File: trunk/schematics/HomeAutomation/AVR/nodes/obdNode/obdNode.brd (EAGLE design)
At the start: 37.4 x 24 mm, 30 parts, among them IC1 MCP2515, IC2 TH8056KDC-AAA-008-RE, IC3 AMIS42665, IC4 ATMEGA64-TQFP32TQFP32, IC5 LM2674, X1 AVRISP6PINHEADER, X2 MICROMATCH-6

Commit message: Work on obdNode
git-svn-id: http://svn.arune.se/svn/hardware@888 bbe6898a-5d1e-0410-8d97-fea9c15d82f3
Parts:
- added C4: 100n, rcl:C0402
- R1, R4: value 10k -> (none)
- moved C12 2.24 mm to (26.0, 42.7)
- moved IC1 2.24 mm to (21.2, 39.9)
- moved R1 2.24 mm to (26.0, 41.6)
- moved IC5 0.71 mm to (32.1, 35.5)
- moved L1 0.41 mm to (38.5, 37.1)
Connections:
- net GND: now also C4.2
- net VBAT: now also C4.1
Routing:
- net GND: track 31.7 -> 36.2 mm, vias 36 -> 38
- net MISO: track 19.8 -> 17.6 mm
- net VBAT: track 26.4 -> 24.9 mm, vias 1 -> 0
- net CLK: track 5.63 -> 4.70 mm
- net CS: track 20.6 -> 19.6 mm
- net SCK: track 17.7 -> 16.7 mm
- net MOSI: track 25.6 -> 24.7 mm
- net INT: track 24.5 -> 23.5 mm
- net TXCAN2: track 12.1 -> 11.2 mm
- net VCC: track 74.6 -> 75.2 mm
- net RXCAN2: track 18.9 -> 18.4 mm

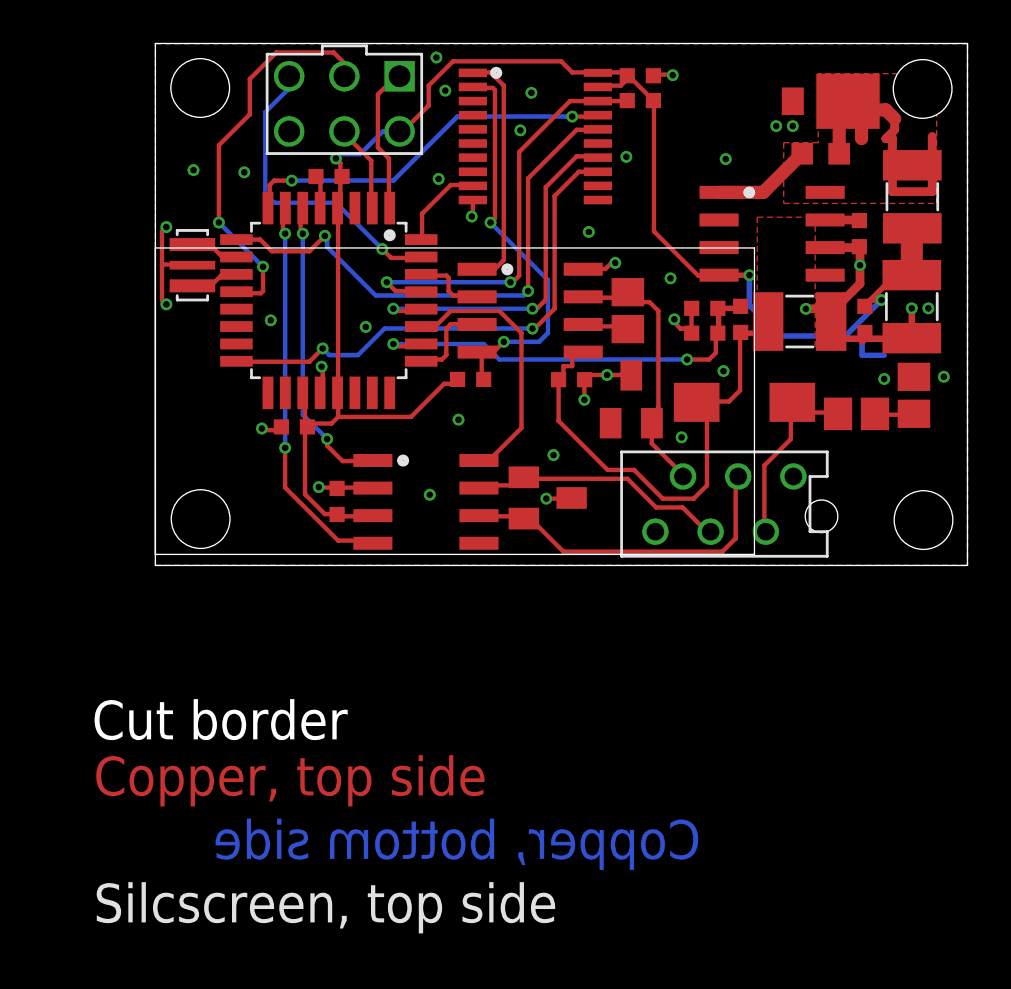
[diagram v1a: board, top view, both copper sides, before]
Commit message: Minor layout improvements
git-svn-id: http://svn.arune.se/svn/hardware@889 bbe6898a-5d1e-0410-8d97-fea9c15d82f3
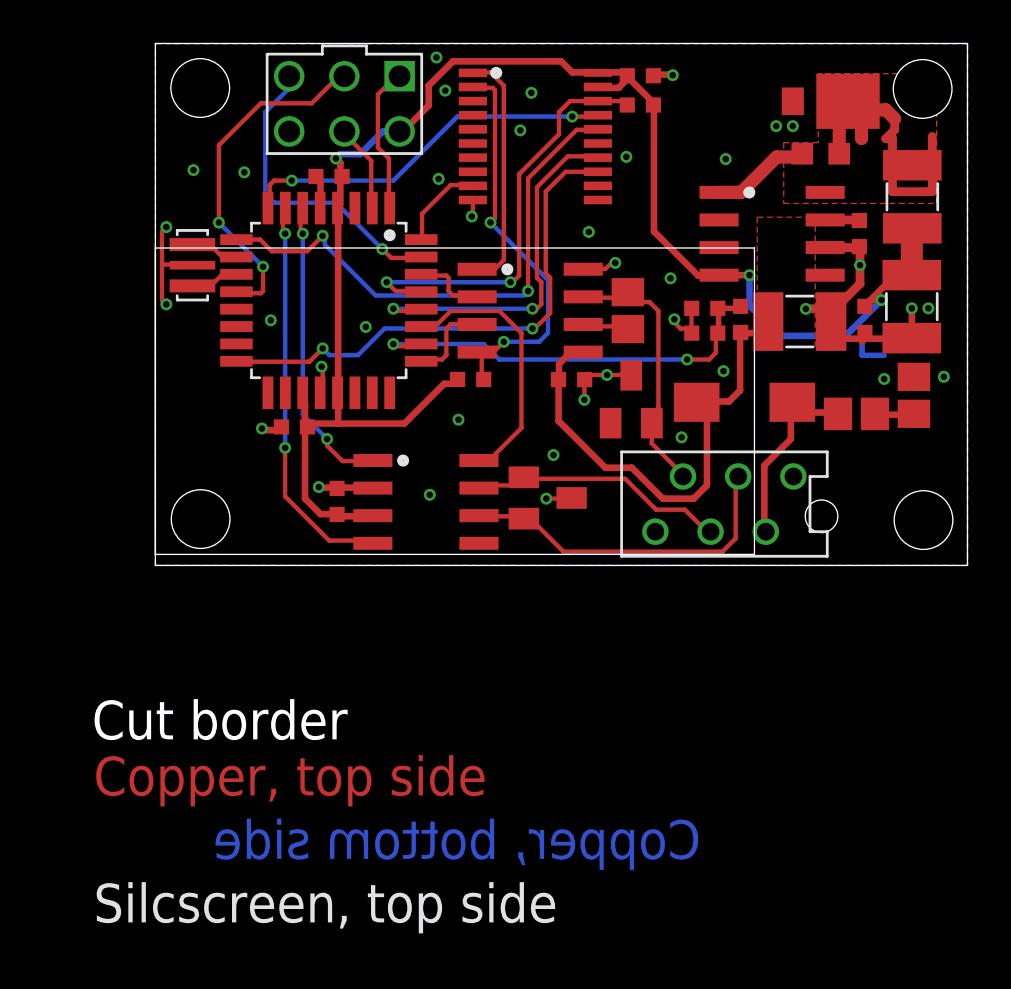
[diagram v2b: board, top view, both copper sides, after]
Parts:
- moved R1 0.20 mm to (26.0, 41.4)
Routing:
- net SCK_A: track 18.2 -> 16.0 mm
- net VCC: track 75.2 -> 75.9 mm
- net INT: track 23.5 -> 24.1 mm

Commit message: Updated version of core module with  - a cheaper PSU  - ISP-contacts as board-edge-connectors
git-svn-id: http://svn.arune.se/svn/hardware@891 bbe6898a-5d1e-0410-8d97-fea9c15d82f3
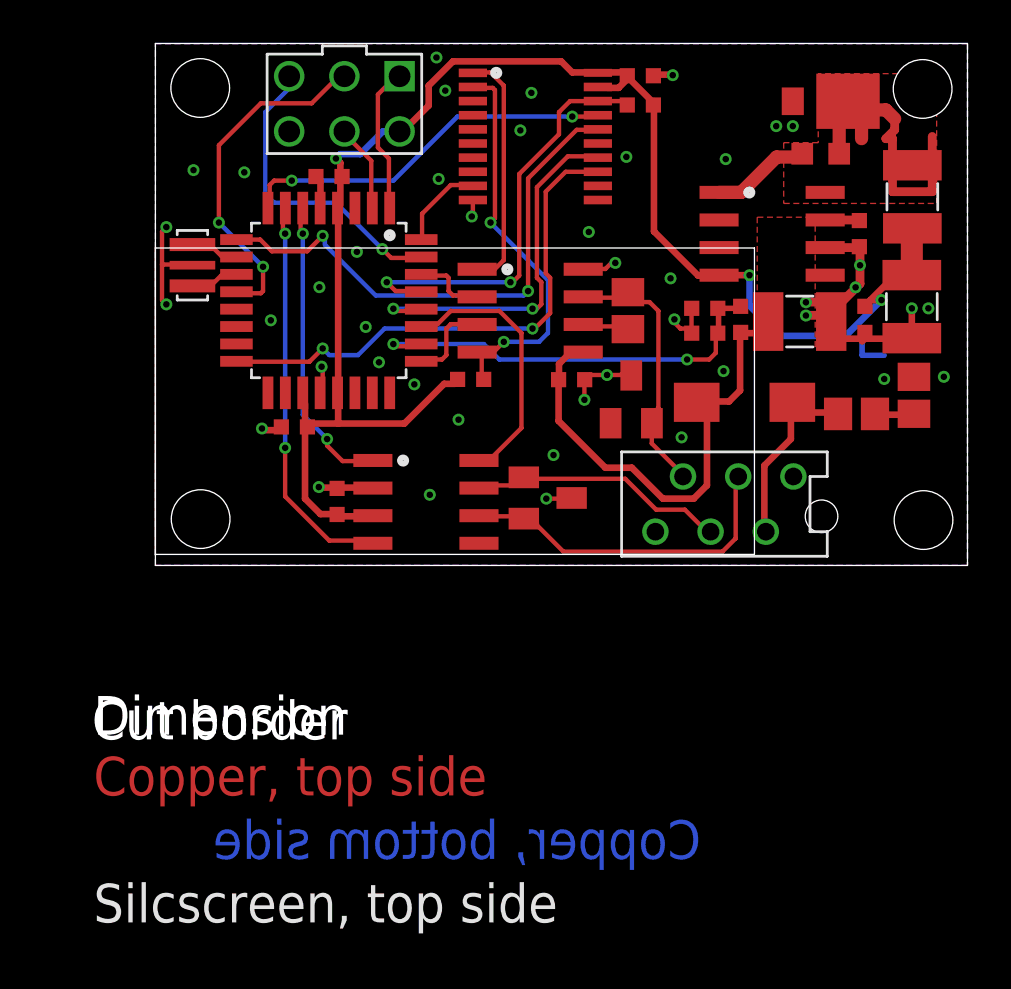
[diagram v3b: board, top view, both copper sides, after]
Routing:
- net GND: track 36.2 -> 37.3 mm, vias 38 -> 44
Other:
- board text added: "Dimension"
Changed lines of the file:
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@@
 <wire x1="36.431" y1="36.4744" x2="35.669" y2="36.4744" width="0.0762" layer="49"/>
 <wire x1="35.669" y1="36.4744" x2="35.669" y2="34.4424" width="0.0762" layer="49"/>
+<text x="0.8382" y="12.4079" size="1.778" layer="20" ratio="10">Dimension</text>
 </plain>
 <attributes>
@@
 <wire x1="36.195" y1="29.863" x2="36.195" y2="30.625" width="0.254" layer="16"/>
 <wire x1="36.195" y1="29.863" x2="37.211" y2="29.863" width="0.254" layer="16"/>
-<via x="33.609" y="31.995" extent="1-16" drill="0.3"/>
+<via x="33.609" y="32.2998" extent="1-16" drill="0.3"/>
 <via x="33.006" y="40.404" extent="1-16" drill="0.3"/>
 <via x="36.0982" y="34.0032" extent="1-16" drill="0.3"/>
@@
 <via x="27.4828" y="42.7482" extent="1-16" drill="0.3"/>
 <via x="16.7132" y="37.973" extent="1-16" drill="0.3"/>
-<polygon width="0.2032" layer="16" isolate="0.1524" rank="3">
+<polygon width="0.2032" layer="16" isolate="0.2032" rank="3">
 <vertex x="41.042" y="44.198"/>
 <vertex x="41.042" y="20.201"/>
@@
 <vertex x="3.683" y="44.198"/>
 </polygon>
-<polygon width="0.2032" layer="1" isolate="0.1524" rank="3">
+<polygon width="0.2032" layer="1" isolate="0.2032" rank="3">
 <vertex x="41.042" y="44.198"/>
 <vertex x="41.042" y="20.201"/>
@@
 <wire x1="36.0982" y1="34.8282" x2="36.0982" y2="33.1518" width="0.4064" layer="1"/>
 <wire x1="36.0982" y1="33.1518" x2="34.8488" y2="31.9024" width="0.4064" layer="1"/>
-<wire x1="33.6296" y1="32.004" x2="34.7472" y2="32.004" width="0.4064" layer="1"/>
+<wire x1="33.6296" y1="32.3088" x2="34.7472" y2="32.3088" width="0.4064" layer="1"/>
 <via x="20.4724" y="40.2082" extent="1-16" drill="0.3"/>
 <via x="16.6116" y="43.561" extent="1-16" drill="0.3"/>
+<via x="15.5956" y="28.5242" extent="1-16" drill="0.3"/>
+<via x="13.97" y="29.5402" extent="1-16" drill="0.3"/>
+<via x="12.954" y="34.6202" extent="1-16" drill="0.3"/>
+<via x="11.2268" y="32.9946" extent="1-16" drill="0.3"/>
+<via x="33.609" y="31.6902" extent="1-16" drill="0.3"/>
+<wire x1="33.6296" y1="31.6992" x2="34.7472" y2="31.6992" width="0.4064" layer="1"/>
+<via x="35.895" y="32.9872" extent="1-16" drill="0.3"/>
 </signal>
 <signal name="VCC">
